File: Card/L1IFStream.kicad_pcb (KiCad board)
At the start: 4 copper layers, 88.9 x 50.8 mm, 111 parts, among them J1 Conn_Coaxial, J2 USB_A, J3 RF_Shield_One_Piece, J4 Conn_Coaxial, U1 MAX2769BETI+T, U10 74LVC374, U11 74HC2GU04, U2 TPS717285DCK, U3 TPS717285DCK, U4 NCP164CSN330T1G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

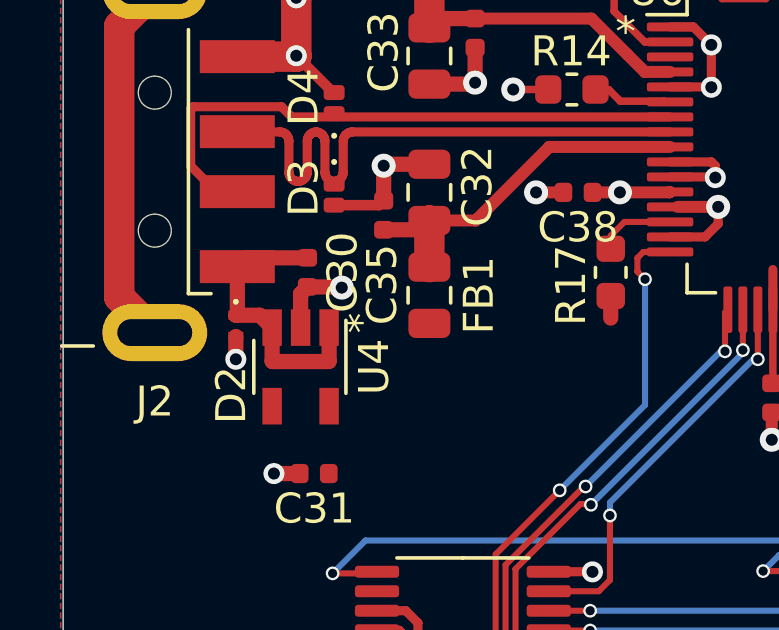
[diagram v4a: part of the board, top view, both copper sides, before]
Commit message: Library clean up through U4
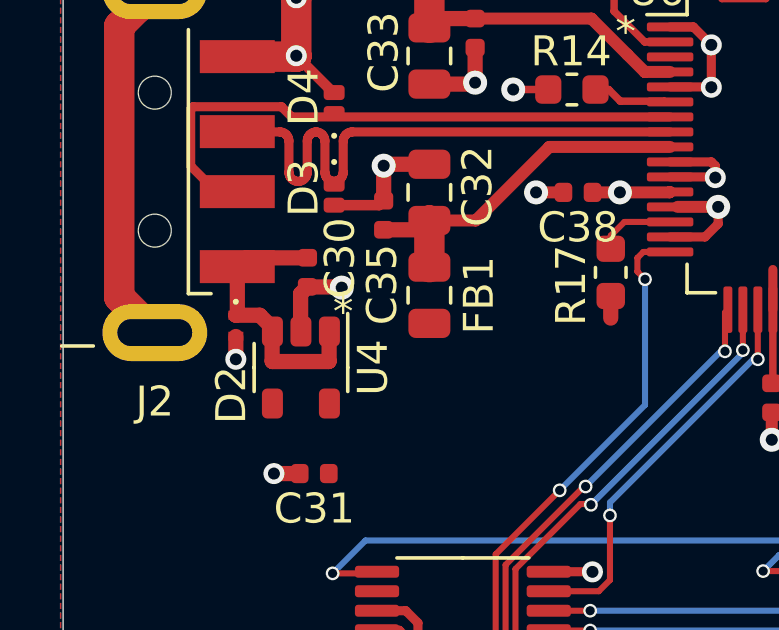
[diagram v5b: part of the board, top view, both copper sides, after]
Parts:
- U4: value NCP164CSN330T1G -> NCP164; footprint L1IFStream:TSOT-23-5 -> L1IF:TSOP-5
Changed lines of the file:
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@@
     )
   )
-  (footprint "L1IFStream:TSOT-23-5" (layer "F.Cu")
-    (at 97.7392 105.0036 -90)
-    (descr "5-pin TSOT23 package, http://cds.linear.com/docs/en/packaging/SOT_5_05-08-1635.pdf")
-    (tags "TSOT-23-5")
-    (property "Alternate" "https://www.diodes.com/assets/Datasheets/AP2127.pdf")
-    (property "Description" "LDO 300 MA AD 3.3V, ULTRA")
-    (property "MPN" "NCP164CSN330T1G")
-    (property "Manufacturer" "Onsemi")
-    (property "Notes" "Alternate: AP2127K-ADJTRG1DIDKR-ND")
-    (property "Sheetfile" "L1IFStream.kicad_sch")
-    (property "Sheetname" "")
-    (property "Vendor" "DigiKey")
-    (property "Vendor P/N#" "488-NCP164CSN330T1GCT-ND")
-    (attr smd)
-    (fp_text reference "U4" (at 0 -2.45 90) (layer "F.SilkS")
-        (effects (font (size 1 1) (thickness 0.15)))
-    )
-    (fp_text value "NCP164CSN330T1G" (at 0 2.5 90) (layer "F.Fab")
-        (effects (font (size 1 1) (thickness 0.15)))
-    )
-    (fp_text user "*" (at -1.8034 -0.9652 -90 unlocked) (layer "F.SilkS")
-        (effects (font (size 1 1) (thickness 0.1)) (justify left bottom))
-    )
-    (fp_text user "${REFERENCE}" (at 0 0) (layer "F.Fab")
-        (effects (font (size 0.5 0.5) (thickness 0.075)))
-    )
-    (fp_line (start -0.88 1.56) (end 0.88 1.56)
-      (stroke (width 0.12) (type solid)) (layer "F.SilkS"))
-    (fp_line (start 0.88 -1.51) (end -1.55 -1.51)
-      (stroke (width 0.12) (type solid)) (layer "F.SilkS"))
-    (fp_line (start -2.17 -1.7) (end -2.17 1.7)
-      (stroke (width 0.05) (type solid)) (layer "F.CrtYd"))
-    (fp_line (start -2.17 -1.7) (end 2.17 -1.7)
-      (stroke (width 0.05) (type solid)) (layer "F.CrtYd"))
-    (fp_line (start 2.17 1.7) (end -2.17 1.7)
-      (stroke (width 0.05) (type solid)) (layer "F.CrtYd"))
-    (fp_line (start 2.17 1.7) (end 2.17 -1.7)
-      (stroke (width 0.05) (type solid)) (layer "F.CrtYd"))
-    (fp_line (start -0.88 -1) (end -0.88 1.45)
-      (stroke (width 0.1) (type solid)) (layer "F.Fab"))
-    (fp_line (start -0.88 -1) (end -0.43 -1.45)
-      (stroke (width 0.1) (type solid)) (layer "F.Fab"))
-    (fp_line (start 0.88 -1.45) (end -0.43 -1.45)
-      (stroke (width 0.1) (type solid)) (layer "F.Fab"))
-    (fp_line (start 0.88 -1.45) (end 0.88 1.45)
-      (stroke (width 0.1) (type solid)) (layer "F.Fab"))
-    (fp_line (start 0.88 1.45) (end -0.88 1.45)
-      (stroke (width 0.1) (type solid)) (layer "F.Fab"))
-    (pad "1" smd rect (at -1.31 -0.95 270) (size 1.22 0.65) (layers "F.Cu" "F.Paste" "F.Mask")
-      (net 86 "Net-(D2-K)") (pinfunction "IN") (pintype "power_in"))
-    (pad "2" smd rect (at -1.31 0 270) (size 1.22 0.65) (layers "F.Cu" "F.Paste" "F.Mask")
-      (net 4 "GND") (pinfunction "GND") (pintype "power_in"))
-    (pad "3" smd rect (at -1.31 0.95 270) (size 1.22 0.65) (layers "F.Cu" "F.Paste" "F.Mask")
-      (net 86 "Net-(D2-K)") (pinfunction "EN") (pintype "input"))
-    (pad "4" smd rect (at 1.31 0.95 270) (size 1.22 0.65) (layers "F.Cu" "F.Paste" "F.Mask")
-      (net 38 "unconnected-(U4-NC-Pad4)") (pinfunction "NC") (pintype "no_connect"))
-    (pad "5" smd rect (at 1.31 -0.95 270) (size 1.22 0.65) (layers "F.Cu" "F.Paste" "F.Mask")
-      (net 21 "+3V3") (pinfunction "OUT") (pintype "power_out"))
-    (model "${KISYS3DMOD}/Package_TO_SOT_SMD.3dshapes/TSOT-23-5.wrl"
-      (offset (xyz 0 0 0))
-      (scale (xyz 1 1 1))
-      (rotate (xyz 0 0 0))
-    )
-  )
   (footprint "L1IFStream:LQFP-64_10x10mm_P0.5mm" (layer "F.Cu")
     (at 115.731 97.422)
@@
     (property "Sheetname" "")
     (attr smd)
-    (fp_text reference "C30" (at 0 -1.17 90) (layer "F.SilkS")
+    (fp_text reference "C30" (at -0.4766 -1.0822 90) (layer "F.SilkS")
         (effects (font (size 1 1) (thickness 0.15)))
     )
@@
       (offset (xyz 0 0 0))
       (scale (xyz 1 1 1))
+      (rotate (xyz 0 0 0))
+    )
+  )
+  (footprint "L1IF:TSOP-5" (layer "F.Cu")
+    (at 97.75 105.025 -90)
+    (descr "SOT, 5 Pin (https://www.jedec.org/sites/default/files/docs/Mo-178c.PDF variant AA), generated with kicad-footprint-generator ipc_gullwing_generator.py")
+    (tags "SOT TO_SOT_SMD")
+    (property "MPN" "NCP164CSN330T1G")
+    (property "Manufacturer" "Onsemi")
+    (property "Sheetfile" "L1IFStream.kicad_sch")
+    (property "Sheetname" "")
+    (property "Vendor" "DigiKey")
+    (property "Vendor PN" "488-NCP164CSN330T1GCT-ND")
+    (property "ki_description" "300mA, Low Noise, Linear Regulator, 1.6-5.0V input voltage range, 3.3V fixed positive output, TSOT-23-5")
+    (property "ki_keywords" "linear regulator ldo fixed positive")
+    (attr smd)
+    (fp_text reference "U4" (at 0 -2.4 90) (layer "F.SilkS")
+        (effects (font (size 1 1) (thickness 0.15)))
+    )
+    (fp_text value "NCP164" (at 0 2.4 90) (layer "F.Fab")
+        (effects (font (size 1 1) (thickness 0.15)))
+    )
+    (fp_text user "*" (at -2.925 -1.75 -180 unlocked) (layer "F.SilkS")
+        (effects (font (size 1 1) (thickness 0.15)) (justify left bottom))
+    )
+    (fp_text user "${REFERENCE}" (at 0 0 90) (layer "F.Fab")
+        (effects (font (size 0.4 0.4) (thickness 0.06)))
+    )
+    (fp_line (start 0 -1.56) (end -1.8 -1.56)
+      (stroke (width 0.12) (type solid)) (layer "F.SilkS"))
+    (fp_line (start 0 -1.56) (end 0.8 -1.56)
+      (stroke (width 0.12) (type solid)) (layer "F.SilkS"))
+    (fp_line (start 0 1.56) (end -0.8 1.56)
+      (stroke (width 0.12) (type solid)) (layer "F.SilkS"))
+    (fp_line (start 0 1.56) (end 0.8 1.56)
+      (stroke (width 0.12) (type solid)) (layer "F.SilkS"))
+    (fp_line (start -2.05 -1.7) (end -2.05 1.7)
+      (stroke (width 0.05) (type solid)) (layer "F.CrtYd"))
+    (fp_line (start -2.05 1.7) (end 2.05 1.7)
+      (stroke (width 0.05) (type solid)) (layer "F.CrtYd"))
+    (fp_line (start 2.05 -1.7) (end -2.05 -1.7)
+      (stroke (width 0.05) (type solid)) (layer "F.CrtYd"))
+    (fp_line (start 2.05 1.7) (end 2.05 -1.7)
+      (stroke (width 0.05) (type solid)) (layer "F.CrtYd"))
+    (fp_line (start -0.8 -1.05) (end -0.4 -1.45)
+      (stroke (width 0.1) (type solid)) (layer "F.Fab"))
+    (fp_line (start -0.8 1.45) (end -0.8 -1.05)
+      (stroke (width 0.1) (type solid)) (layer "F.Fab"))
+    (fp_line (start -0.4 -1.45) (end 0.8 -1.45)
+      (stroke (width 0.1) (type solid)) (layer "F.Fab"))
+    (fp_line (start 0.8 -1.45) (end 0.8 1.45)
+      (stroke (width 0.1) (type solid)) (layer "F.Fab"))
+    (fp_line (start 0.8 1.45) (end -0.8 1.45)
+      (stroke (width 0.1) (type solid)) (layer "F.Fab"))
+    (pad "1" smd roundrect (at -1.2 -0.95 270) (size 1 0.7) (layers "F.Cu" "F.Paste" "F.Mask") (roundrect_rratio 0.25)
+      (net 86 "Net-(D2-K)") (pinfunction "IN") (pintype "power_in"))
+    (pad "2" smd roundrect (at -1.2 0 270) (size 1 0.7) (layers "F.Cu" "F.Paste" "F.Mask") (roundrect_rratio 0.25)
+      (net 4 "GND") (pinfunction "GND") (pintype "power_in"))
+    (pad "3" smd roundrect (at -1.2 0.95 270) (size 1 0.7) (layers "F.Cu" "F.Paste" "F.Mask") (roundrect_rratio 0.25)
+      (net 86 "Net-(D2-K)") (pinfunction "EN") (pintype "input"))
+    (pad "4" smd roundrect (at 1.2 0.95 270) (size 1 0.7) (layers "F.Cu" "F.Paste" "F.Mask") (roundrect_rratio 0.25)
+      (net 38 "unconnected-(U4-NC-Pad4)") (pinfunction "NC") (pintype "no_connect"))
+    (pad "5" smd roundrect (at 1.2 -0.95 270) (size 1 0.7) (layers "F.Cu" "F.Paste" "F.Mask") (roundrect_rratio 0.25)
+      (net 21 "+3V3") (pinfunction "OUT") (pintype "power_out"))
+    (model "${KICAD6_3DMODEL_DIR}/Package_TO_SOT_SMD.3dshapes/SOT-23-5.wrl"
+      (offset (xyz 0 0 0))
+      (scale (xyz 1 1 1))

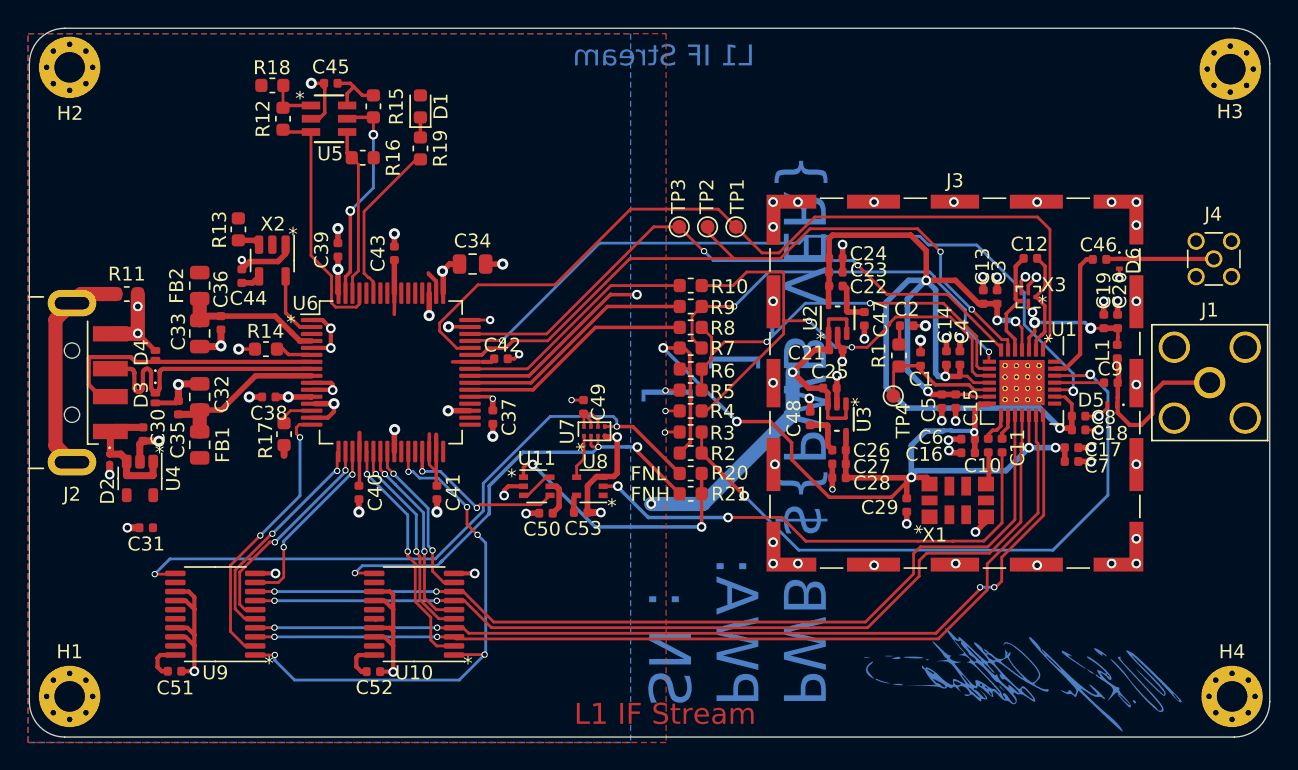
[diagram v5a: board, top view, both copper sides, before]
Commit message: Library cleaned up except for Rs and Cs
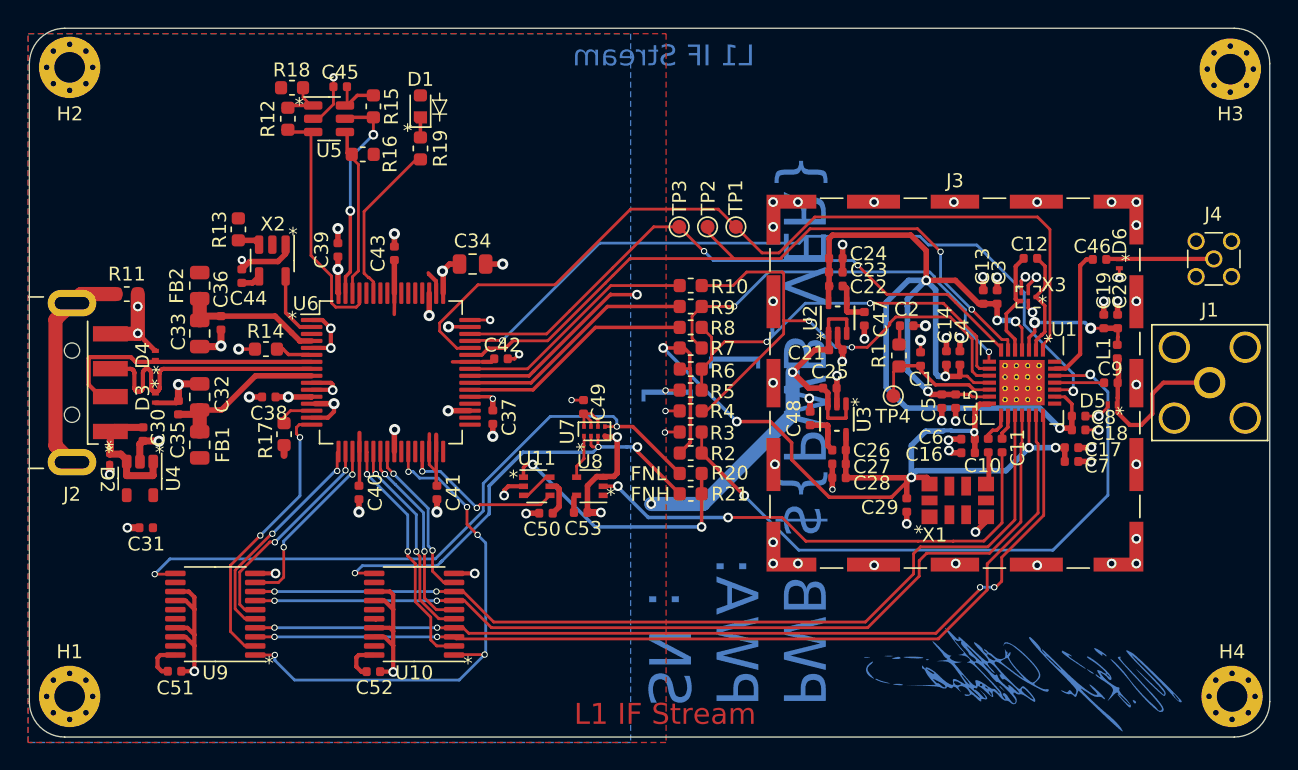
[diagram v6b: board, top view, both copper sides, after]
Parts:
- D1: footprint L1IFStream:LED_0603_1608Metric -> L1IF:LED_0603_1608Metric
- D2, D5, D6: footprint L1IFStream:Texas_DPY0002A_0.6x1mm_P0.65mm -> L1IF:Texas_DPY0002A_0.6x1mm_P0.65mm
- D3, D4: footprint L1IFStream:DPY-PX1SON_1.0mmx0.6mm -> L1IF:Texas_DPY0002A_0.6x1mm_P0.65mm
- FB1, FB2: footprint L1IFStream:C_0805_2012Metric -> L1IF:C_0805_2012Metric
- H1, H2, H3, H4: footprint L1IFStream:MountingHole_2.2mm_M2_Pad_Via -> L1IF:MountingHole_2.2mm_M2_Pad_Via
- J1: footprint L1IFStream:SMA_Amphenol_132203-12_Horizontal -> L1IF:SMA_Amphenol_132203-12_Horizontal
- J2: footprint L1IFStream:USB_A_CNCTech_1001-011-01101_Horizontal -> L1IF:USB_A_CNCTech_1001-011-01101_Horizontal
- J3: footprint L1IFStream:Laird_Technologies_BMI-S-103_26.21x26.21mm -> L1IF:Laird_Technologies_BMI-S-103_26.21x26.21mm
- J4: footprint L1IFStream:MMCX_Molex_73415-1471_Vertical -> L1IF:MMCX_Molex_73415-1471_Vertical
- L1: footprint L1IFStream:L_0402_1005Metric -> L1IF:L_0402_1005Metric
- TP1, TP2, TP3, TP4: footprint L1IFStream:TestPoint_Pad_D1.0mm -> L1IF:TestPoint_Pad_D1.0mm
- U10, U9: footprint L1IFStream:TSSOP-20_4.4x6.5mm_P0.65mm -> L1IF:TSSOP-20_4.4x6.5mm_P0.65mm
- U11: footprint L1IFStream:SOT-363_SC-70-6 -> L1IF:SOT-363_SC-70-6
- U5: footprint L1IFStream:93LC66BT-I&slash_OT -> L1IF:SOT-23-6
- U6: footprint L1IFStream:LQFP-64_10x10mm_P0.5mm -> L1IF:LQFP-64_10x10mm_P0.5mm
- U7: footprint L1IFStream:SOT-833-1 -> L1IF:SOT-833-1
- U8: footprint L1IFStream:SOT-353_SC-70-5 -> L1IF:SOT-353_SC-70-5
- moved R18 1.42 mm to (108.7, 77.0)
- moved C45 0.71 mm to (112.1, 77.0)
- moved R12 0.35 mm to (108.3, 79.2)
- moved R16 0.24 mm to (113.7, 81.8)
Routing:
- net +3V3: track 71.1 -> 70.2 mm

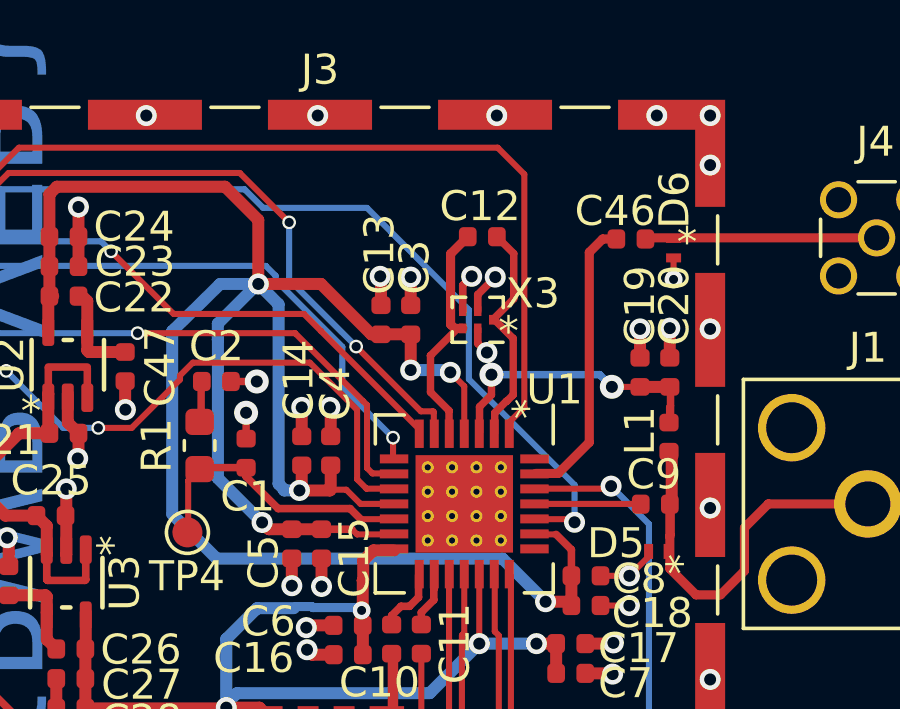
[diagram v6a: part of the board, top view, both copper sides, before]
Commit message: Capacitor silk placement
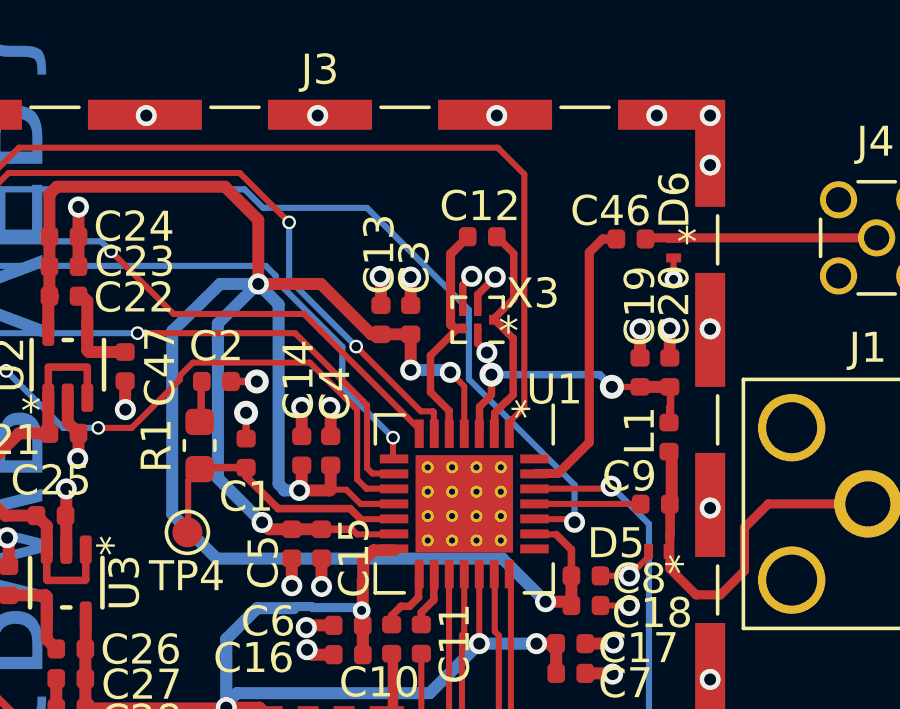
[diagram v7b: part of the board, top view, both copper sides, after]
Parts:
- C1, C2, C46, C9: footprint L1IFStream:C_0402_1005Metric -> L1IF:C_0402_1005Metric
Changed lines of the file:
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@@
     )
   )
-  (footprint "L1IFStream:C_0402_1005Metric" (layer "F.Cu")
+  (footprint "L1IF:C_0402_1005Metric" (layer "F.Cu")
     (at 167.335 98.171 180)
     (descr "Capacitor SMD 0402 (1005 Metric), square (rectangular) end terminal, IPC_7351 nominal, (Body size source: http://www.tortai-tech.com/upload/download/2011102023233369053.pdf), generated with kicad-footprint-generator")
     (tags "capacitor")
     (property "Description" "CAP CER 470PF 50V C0G/NP0 0402 10%")
-    (property "Digi-Key" "490-6242-1-ND")
+    (property "MPN" "GRM1555C1H471JA01J")
+    (property "Manufacturer" "Murata Electronics")
     (property "Sheetfile" "L1IFStream.kicad_sch")
     (property "Sheetname" "")
+    (property "Vendor" "DigiKey")
+    (property "Vendor PN" "490-6242-6-ND")
     (attr smd)
-    (fp_text reference "C9" (at 0.0506 0.9906 180) (layer "F.SilkS")
+    (fp_text reference "C9" (at 0.86 0.921) (layer "F.SilkS")
         (effects (font (size 1 1) (thickness 0.15)))
     )
@@
     )
   )
-  (footprint "L1IFStream:C_0402_1005Metric" (layer "F.Cu")
+  (footprint "L1IF:C_0402_1005Metric" (layer "F.Cu")
     (at 153.6954 96.4716 90)
     (descr "Capacitor SMD 0402 (1005 Metric), square (rectangular) end terminal, IPC_7351 nominal, (Body size source: http://www.tortai-tech.com/upload/download/2011102023233369053.pdf), generated with kicad-footprint-generator")
     (tags "capacitor")
     (property "Description" "CAP CER 27PF 50V C0G/NP0 0402 5%")
-    (property "Digi-Key" "490-12651-1-ND")
+    (property "MPN" "GCM1555C1H270JA16D")
+    (property "Manufacturer" "Murata Electronics")
     (property "Sheetfile" "L1IFStream.kicad_sch")
     (property "Sheetname" "")
+    (property "Vendor" "DigiKey")
+    (property "Vendor PN" "490-12651-1-ND")
     (attr smd)
-    (fp_text reference "C1" (at -1.4454 0.0508 180) (layer "F.SilkS")
+    (fp_text reference "C1" (at -1.4534 0.0046 180) (layer "F.SilkS")
         (effects (font (size 1 1) (thickness 0.15)))
     )
@@
     )
   )
-  (footprint "L1IFStream:C_0402_1005Metric" (layer "F.Cu")
+  (footprint "L1IF:C_0402_1005Metric" (layer "F.Cu")
     (at 166.5224 89.3318 180)
     (descr "Capacitor SMD 0402 (1005 Metric), square (rectangular) end terminal, IPC_7351 nominal, (Body size source: http://www.tortai-tech.com/upload/download/2011102023233369053.pdf), generated with kicad-footprint-generator")
     (tags "capacitor")
     (property "Description" "CAP CER 470PF 50V C0G/NP0 0402 10%")
-    (property "Digi-Key" "490-6242-1-ND")
+    (property "MPN" "GRM1555C1H471JA01J")
+    (property "Manufacturer" "Murata Electronics")
     (property "Sheetfile" "L1IFStream.kicad_sch")
     (property "Sheetname" "")
+    (property "Vendor" "DigiKey")
+    (property "Vendor PN" "490-6242-6-ND")
     (attr smd)
-    (fp_text reference "C46" (at 0.5224 0.9318) (layer "F.SilkS")
+    (fp_text reference "C46" (at 0.6724 0.9318) (layer "F.SilkS")
         (effects (font (size 1 1) (thickness 0.15)))
     )
-    (fp_text value "470 pF" (at 0 1.17) (layer "F.Fab")
+    (fp_text value "470 pF" (at 0 1.17 180) (layer "F.Fab")
         (effects (font (size 1 1) (thickness 0.15)))
     )
-    (fp_text user "${REFERENCE}" (at 0 0) (layer "F.Fab")
+    (fp_text user "${REFERENCE}" (at 0 0 180) (layer "F.Fab")
         (effects (font (size 0.25 0.25) (thickness 0.04)))
     )
@@
     )
   )
-  (footprint "L1IFStream:C_0402_1005Metric" (layer "F.Cu")
+  (footprint "L1IF:C_0402_1005Metric" (layer "F.Cu")
     (at 152.705 94.0816)
     (descr "Capacitor SMD 0402 (1005 Metric), square (rectangular) end terminal, IPC_7351 nominal, (Body size source: http://www.tortai-tech.com/upload/download/2011102023233369053.pdf), generated with kicad-footprint-generator")
     (tags "capacitor")
     (property "Description" "CAP CER 470PF 50V C0G/NP0 0402 10%")
-    (property "Digi-Key" "490-6242-1-ND")
+    (property "MPN" "GRM1555C1H471JA01J")
+    (property "Manufacturer" "Murata Electronics")
     (property "Sheetfile" "L1IFStream.kicad_sch")
     (property "Sheetname" "")
+    (property "Vendor" "DigiKey")
+    (property "Vendor PN" "490-6242-6-ND")
     (attr smd)
     (fp_text reference "C2" (at 0 -1.17) (layer "F.SilkS")
